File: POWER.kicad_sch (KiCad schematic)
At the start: 44 parts, among them U4 LMR43620R5RPER, U5 LMR604303SRAKRQ1, U6 AP7361C-33FGE-7, U7 AP7361C-33FGE-7

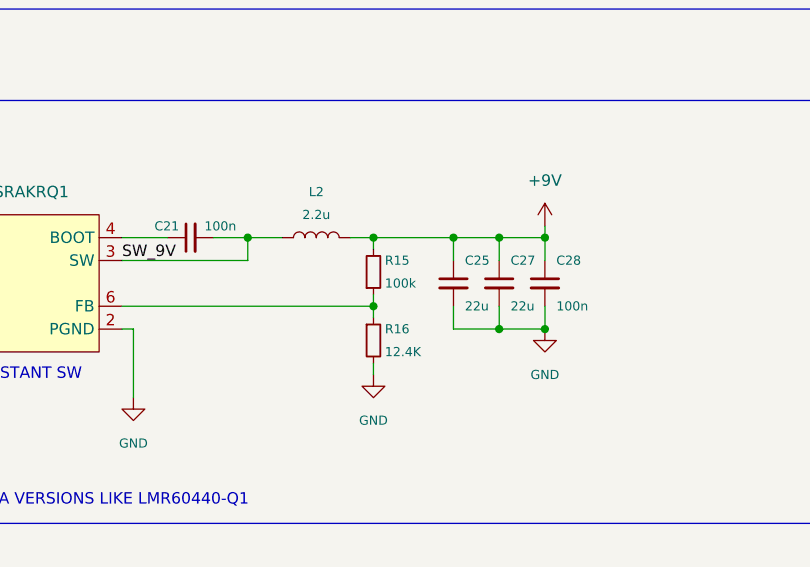
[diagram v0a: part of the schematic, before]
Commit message: BOM complete and JLC prod files generated
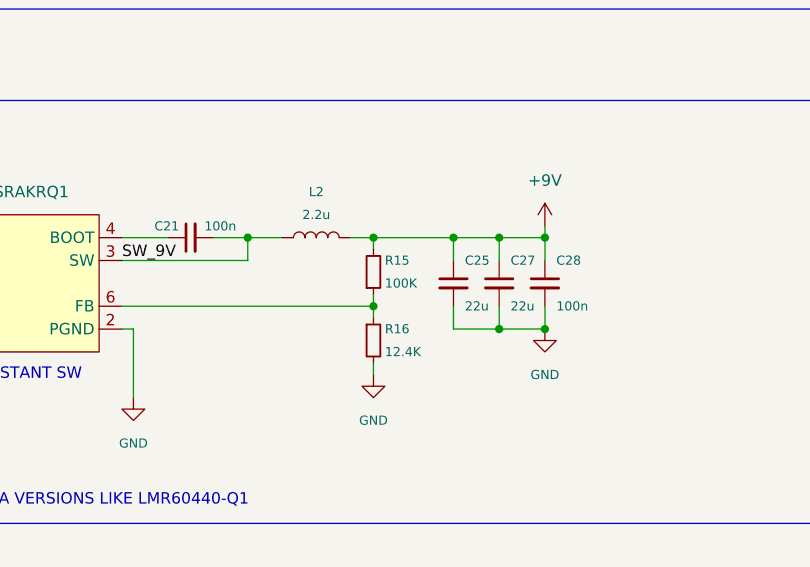
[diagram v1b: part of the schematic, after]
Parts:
- C13, C14: LCSC (none) -> C440198
- C15, C16: LCSC (none) -> C307331; LCSC Part C1525 -> C307331
- C17, C20, C21, C26, C28: LCSC (none) -> C1525
- C18: LCSC (none) -> C15849
- C22, C24, C25, C27: LCSC (none) -> C45783
- C29, C30, C31, C32: LCSC (none) -> C19666
- D2: LCSC (none) -> C134980
- D3, D4: LCSC (none) -> C2905650
- R10, R19, R20, R8: LCSC (none) -> C25744
- R11: LCSC (none) -> C11702
- R12: LCSC (none) -> C25857
- R15: value 100k -> 100K; LCSC (none) -> C25741
- R16: LCSC (none) -> C11692
- R9: LCSC (none) -> C25741
- U4: LCSC (none) -> C32712896
- U5: LCSC (none) -> C49292342
- U6, U7: LCSC (none) -> C151007

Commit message: nextpcb manufacturing files updated
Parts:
- C13, C14: MPN (none) -> GRM21BR61H106KE43L; Manufacturer (none) -> Murata Electronics
- C15, C16, C17, C20, C21, C26, C28: MPN (none) -> GRM022R60J104KE15D; Manufacturer (none) -> Murata Electronics
- C18: MPN (none) -> CL10A105KB8NNNC; Manufacturer (none) -> Samsung Electro-Mechanics
- C22, C24, C25, C27: MPN (none) -> CL21A226MAQNNNE; Manufacturer (none) -> Samsung Electro-Mechanics
- C29, C30, C31, C32: MPN (none) -> CL10A475KO8NNNC; Manufacturer (none) -> Samsung Electro-Mechanics
- D2: MPN (none) -> SMAJ30CA-13-F; Manufacturer (none) -> Diodes Incorporated
- D3, D4: MPN (none) -> 1N5819W; Manufacturer (none) -> TECH PUBLIC
- L1, L2: MPN (none) -> XGL4020-222MEC; Manufacturer (none) -> Coilcraft
- R10, R19, R20, R8: MPN (none) -> 0402WGF1002TCE; Manufacturer (none) -> UNI-ROYAL(Uniroyal Elec)
- R11: MPN (none) -> 0402WGF1001TCE; Manufacturer (none) -> UNI-ROYAL(Uniroyal Elec)
- R12: MPN (none) -> 0402WGF1652TCE; Manufacturer (none) -> UNI-ROYAL(Uniroyal Elec)
- R15, R9: MPN (none) -> 0402WGF1003TCE; Manufacturer (none) -> UNI-ROYAL(Uniroyal Elec)
- R16: MPN (none) -> 0402WGF1242TCE; Manufacturer (none) -> UNI-ROYAL(Uniroyal Elec)
